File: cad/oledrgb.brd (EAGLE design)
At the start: 27.5 x 29.5 mm, 17 parts, among them U1 FAN5331SX

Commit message: embiggen connector
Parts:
- removed CN1: (no value), jaw:HEADER-2X04
- added CONN2: HEADER-5X2-PTH, jaw:HEADER-5X2-PTH
- moved R3 2.55 mm to (59.0, 18.5), turned to 180 degrees
- moved C5 0.51 mm to (40.3, 12.5)
- moved C1 0.50 mm to (48.0, 10.5)
- moved C2 0.50 mm to (40.4, 9.00)
- moved C3 0.50 mm to (42.2, 12.5)
- moved C4 0.50 mm to (44.0, 12.5)
- moved D1 0.50 mm to (40.0, 6.00)
- moved L1 0.50 mm to (43.5, 6.00)
- moved R1 0.50 mm to (42.2, 9.00)
- moved R2 0.50 mm to (44.0, 9.00)
- moved U1 0.50 mm to (48.0, 7.50)
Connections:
- new net N$19: CONN2.10
- new net N$4: CONN2.9
- net DPYCS: now also CONN2.7; no longer CN1.7
- net DPYDC: now also CONN2.6; no longer CN1.6
- net GND: now also CONN2.8; no longer CN1.8
- net NRST: now also CONN2.2; no longer CN1.2
- net SPIMISO: now also CONN2.3; no longer CN1.3
- net SPIMOSI: now also CONN2.5; no longer CN1.5
- net SPISCK: now also CONN2.4; no longer CN1.4
- net VCC: now also CONN2.1; no longer CN1.1
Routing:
- net N$20: track 13.4 -> 10.1 mm
- net V12: track 52.2 -> 49.4 mm
- net VCC: track 52.5 -> 54.9 mm
- net DPYDC: track 26.8 -> 25.2 mm
- net DPYCS: track 28.1 -> 26.9 mm
- net SPIMOSI: track 30.3 -> 29.3 mm
- net NRST: track 31.5 -> 30.5 mm
- net SPISCK: track 32.7 -> 31.7 mm
- net GND: track 55.9 -> 56.7 mm
- net N$6: track 14.0 -> 13.5 mm
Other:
- outline, holes or cut-outs redrawn

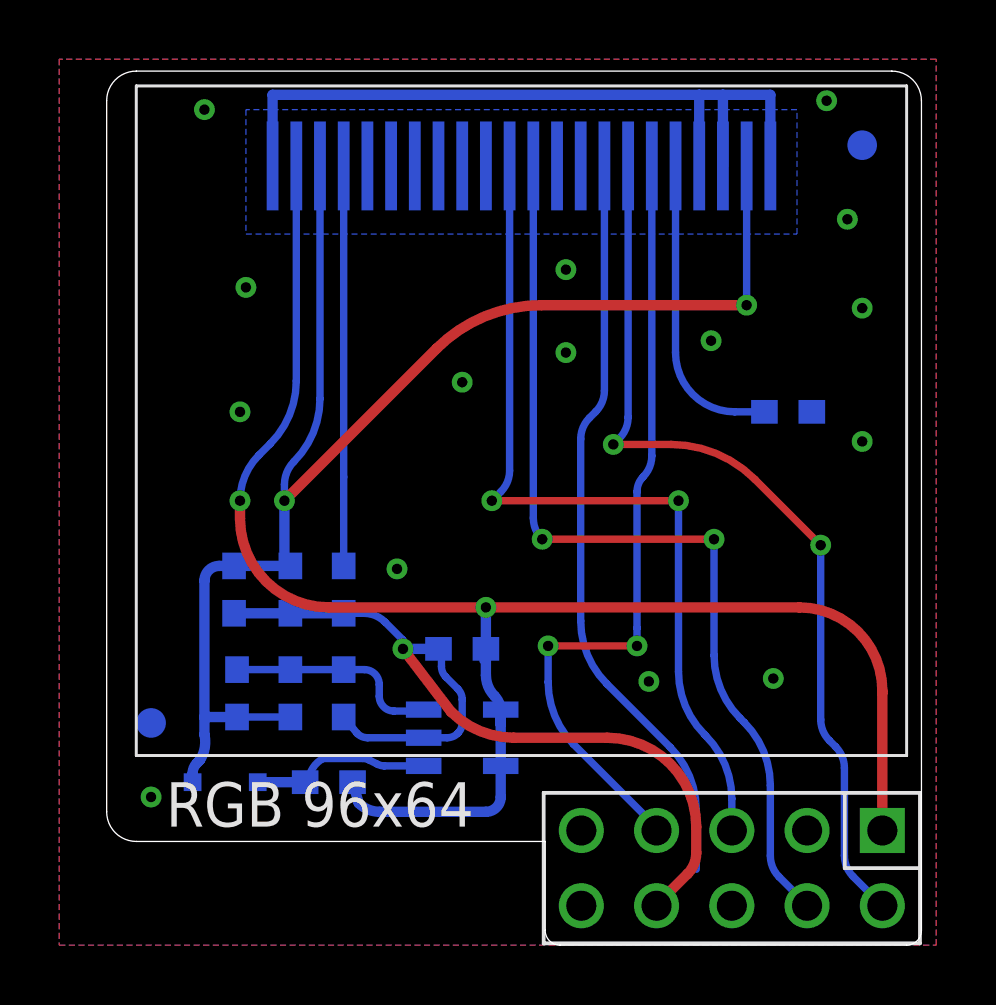
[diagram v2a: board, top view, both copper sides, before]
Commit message: scootch closer to edge
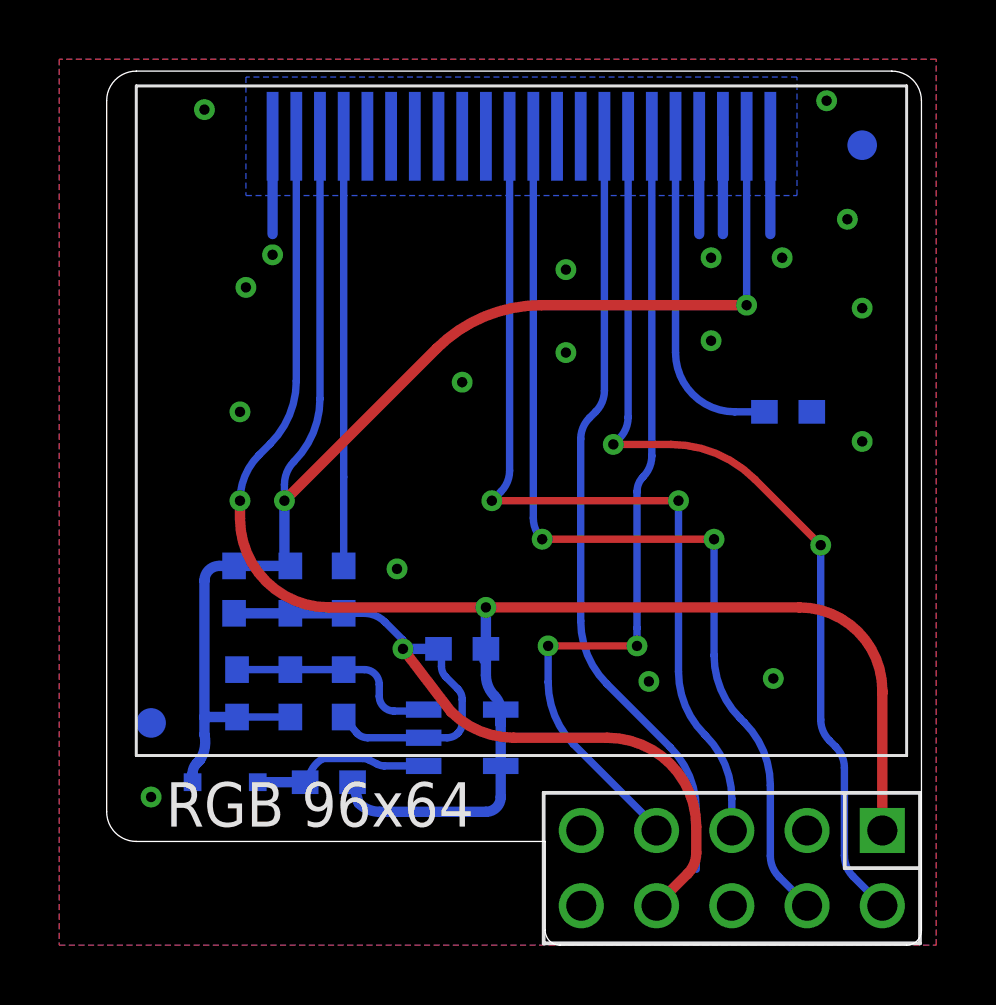
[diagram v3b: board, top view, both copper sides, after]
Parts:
- moved CONN1 1.00 mm to (50.0, 28.0)
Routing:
- net GND: track 56.7 -> 43.5 mm, vias 16 -> 19
- net V12: track 49.4 -> 51.4 mm
- net SPISCK: track 31.7 -> 32.7 mm
- net VCC: track 54.9 -> 55.9 mm
- net SPIMOSI: track 29.3 -> 30.3 mm
- net NRST: track 30.5 -> 31.5 mm
- net N$6: track 13.5 -> 14.5 mm
- net N$20: track 10.1 -> 11.1 mm
- net DPYDC: track 25.2 -> 26.2 mm
- net DPYCS: track 26.9 -> 27.9 mm
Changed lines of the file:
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@@
 <layer number="14" name="Route14" color="1" fill="6" visible="no" active="no"/>
 <layer number="15" name="Route15" color="4" fill="6" visible="no" active="no"/>
-<layer number="16" name="Bottom" color="1" fill="1" visible="no" active="yes"/>
+<layer number="16" name="Bottom" color="1" fill="1" visible="yes" active="yes"/>
 <layer number="17" name="Pads" color="2" fill="1" visible="yes" active="yes"/>
 <layer number="18" name="Vias" color="2" fill="1" visible="yes" active="yes"/>
@@
 <attribute name="VALUE" x="42.586" y="13.978" size="1" layer="28" font="vector" ratio="10" rot="MR270"/>
 </element>
-<element name="CONN1" library="jaw" package="HEADER-22X1-SMD8" value="HEADER-22X1-SMD8" x="50" y="27" rot="MR180"/>
+<element name="CONN1" library="jaw" package="HEADER-22X1-SMD8" value="HEADER-22X1-SMD8" x="50" y="28" rot="MR180"/>
 <element name="D1" library="jaw" package="SOD-323" value="DIODESOD-323" x="40" y="6" smashed="yes" rot="MR180">
 <attribute name="NAME" x="38" y="5.5" size="1" layer="26" ratio="10" rot="MR0"/>
@@
 <wire x1="49.742640625" y1="7.5" x2="47.621321875" y2="8.378678125" width="0.35" layer="1" curve="-44.999958"/>
 <wire x1="47.621321875" y1="8.378678125" x2="46" y2="10.5" width="0.35" layer="1"/>
-<wire x1="41.6" y1="26.8" x2="41.6" y2="29.2" width="0.35" layer="16"/>
-<wire x1="58.4" y1="26.8" x2="58.4" y2="29.2" width="0.35" layer="16"/>
-<wire x1="41.6" y1="29.2" x2="56" y2="29.2" width="0.35" layer="16"/>
-<wire x1="56" y1="26.8" x2="56" y2="29.2" width="0.35" layer="16"/>
-<wire x1="56" y1="29.2" x2="56.8" y2="29.2" width="0.35" layer="16"/>
-<wire x1="56.8" y1="26.8" x2="56.8" y2="29.2" width="0.35" layer="16"/>
-<wire x1="56.8" y1="29.2" x2="58.4" y2="29.2" width="0.35" layer="16"/>
+<wire x1="41.6" y1="27.8" x2="41.6" y2="24.5" width="0.35" layer="16"/>
+<wire x1="58.4" y1="27.8" x2="58.4" y2="24.5" width="0.35" layer="16"/>
+<wire x1="56" y1="27.8" x2="56" y2="24.5" width="0.35" layer="16"/>
+<wire x1="56.8" y1="27.8" x2="56.8" y2="24.5" width="0.35" layer="16"/>
 <polygon width="0.25" layer="16" spacing="0.8" pour="hatch" isolate="0.25">
 <vertex x="34.4" y="30.4"/>
@@
 <wire x1="47.3" y1="9.90710625" x2="47.3" y2="10.4" width="0.25" layer="16"/>
 <wire x1="47.3" y1="10.4" x2="47.2" y2="10.5" width="0.25" layer="16"/>
-<wire x1="58.4" y1="29.2" x2="60.3" y2="29" width="0" layer="19" extent="16-16"/>
-<wire x1="39.3" y1="28.7" x2="41.6" y2="29.2" width="0" layer="19" extent="16-16"/>
-<wire x1="61" y1="25" x2="58.4" y2="26.8" width="0" layer="19" extent="16-16"/>
-<wire x1="61.5" y1="22" x2="61" y2="25" width="0" layer="19" extent="1-1"/>
-<wire x1="59.8" y1="18.5" x2="61.5" y2="22" width="0" layer="19" extent="16-16"/>
-<wire x1="61.5" y1="17.5" x2="59.8" y2="18.5" width="0" layer="19" extent="16-16"/>
-<wire x1="56.4" y1="20.9" x2="59.8" y2="18.5" width="0" layer="19" extent="16-16"/>
-<wire x1="40.7" y1="22.7" x2="41.6" y2="26.8" width="0" layer="19" extent="16-16"/>
-<wire x1="40.5" y1="18.5" x2="40.7" y2="22.7" width="0" layer="19" extent="1-1"/>
-<wire x1="51.5" y1="20.5" x2="56.4" y2="20.9" width="0" layer="19" extent="1-1"/>
-<wire x1="51.5" y1="23.3" x2="51.5" y2="20.5" width="0" layer="19" extent="1-1"/>
-<wire x1="48" y1="19.5" x2="51.5" y2="20.5" width="0" layer="19" extent="1-1"/>
-<wire x1="45.8" y1="13.2" x2="48" y2="19.5" width="0" layer="19" extent="1-1"/>
-<wire x1="45.39289375" y1="11.40710625" x2="45.8" y2="13.2" width="0" layer="19" extent="16-16"/>
-<wire x1="54.56" y1="1.83" x2="54.6" y2="1.9" width="0" layer="19" extent="1-1"/>
-<wire x1="54.3" y1="9.4" x2="52.9" y2="7.5" width="0" layer="19" extent="1-1"/>
-<wire x1="58.5" y1="9.5" x2="54.3" y2="9.4" width="0" layer="19" extent="1-1"/>
-<wire x1="37.5" y1="5.5" x2="40.3" y2="11.7" width="0" layer="19" extent="16-16"/>
+<via x="41.6" y="23.8" extent="1-16" drill="0.35"/>
+<via x="56.4" y="23.7" extent="1-16" drill="0.35"/>
+<via x="58.8" y="23.7" extent="1-16" drill="0.35"/>
 </signal>
 <signal name="VCC">
@@
 <wire x1="59.38" y1="11.9" x2="62.18" y2="9.1" width="0.35" layer="1" curve="-90"/>
 <via x="48.8" y="11.9" extent="1-16" drill="0.35"/>
-<wire x1="42.4" y1="26.8" x2="42.4" y2="19.542640625" width="0.25" layer="16"/>
+<wire x1="42.4" y1="27.8" x2="42.4" y2="19.542640625" width="0.25" layer="16"/>
 <wire x1="42.4" y1="19.542640625" x2="41.521321875" y2="17.421321875" width="0.25" layer="16" curve="-44.999958"/>
 <wire x1="41.521321875" y1="17.421321875" x2="41.136396875" y2="17.036396875" width="0.25" layer="16"/>
@@
 <wire x1="62.18" y1="9.1" x2="62.18" y2="9" width="0.35" layer="1"/>
 <wire x1="62.18" y1="9" x2="62.18" y2="4.37" width="0.35" layer="1"/>
-<wire x1="62.18" y1="12.12" x2="62.18" y2="9.1" width="0" layer="19" extent="1-16"/>
-<wire x1="62.18" y1="9.1" x2="62.18" y2="9.1" width="0" layer="19" extent="1-16"/>
-<wire x1="62.18" y1="9.1" x2="62.18" y2="9" width="0" layer="19" extent="1-16"/>
-<wire x1="62.18" y1="12.12" x2="62.18" y2="12.491571875" width="0" layer="19" extent="1-16"/>
-<wire x1="62.18" y1="12.491571875" x2="61.5942125" y2="13.9057875" width="0" layer="19" curve="45.000063" extent="1-16"/>
-<wire x1="61.5942125" y1="13.9057875" x2="61.5857875" y2="13.9142125" width="0" layer="19" extent="1-16"/>
-<wire x1="61.5857875" y1="13.9142125" x2="60.171571875" y2="14.5" width="0" layer="19" curve="45.00009" extent="1-16"/>
 </signal>
 <signal name="NRST">
@@
 <wire x1="61.19289375" y1="2.81710625" x2="62.18" y2="1.83" width="0.25" layer="16"/>
 <contactref element="CONN1" pad="16"/>
-<wire x1="53.6" y1="26.8" x2="53.6" y2="18.3142125" width="0.25" layer="16"/>
+<wire x1="53.6" y1="27.8" x2="53.6" y2="18.3142125" width="0.25" layer="16"/>
 <wire x1="53.6" y1="18.3142125" x2="53.30710625" y2="17.60710625" width="0.25" layer="16" curve="-45"/>
 <wire x1="53.30710625" y1="17.60710625" x2="53.1" y2="17.4" width="0.25" layer="16"/>
@@
 <signal name="DPYDC">
 <contactref element="CONN1" pad="15"/>
-<wire x1="52.8" y1="26.8" x2="52.8" y2="19.2142125" width="0.25" layer="16"/>
+<wire x1="52.8" y1="27.8" x2="52.8" y2="19.2142125" width="0.25" layer="16"/>
 <wire x1="52.8" y1="19.2142125" x2="52.50710625" y2="18.50710625" width="0.25" layer="16" curve="-45"/>
 <wire x1="52.50710625" y1="18.50710625" x2="52.29289375" y2="18.29289375" width="0.25" layer="16"/>
@@
 <signal name="SPISCK">
 <contactref element="CONN1" pad="12"/>
-<wire x1="50.4" y1="26.8" x2="50.4" y2="14.9142125" width="0.25" layer="16"/>
+<wire x1="50.4" y1="27.8" x2="50.4" y2="14.9142125" width="0.25" layer="16"/>
 <wire x1="50.4" y1="14.9142125" x2="50.69289375" y2="14.20710625" width="0.25" layer="16" curve="45"/>
 <wire x1="50.69289375" y1="14.20710625" x2="50.7" y2="14.2" width="0.25" layer="16"/>
@@
 <signal name="SPIMOSI">
 <contactref element="CONN1" pad="11"/>
-<wire x1="49.6" y1="26.8" x2="49.6" y2="16.5142125" width="0.25" layer="16"/>
+<wire x1="49.6" y1="27.8" x2="49.6" y2="16.5142125" width="0.25" layer="16"/>
 <wire x1="49.6" y1="16.5142125" x2="49.30710625" y2="15.80710625" width="0.25" layer="16" curve="-45"/>
 <wire x1="49.30710625" y1="15.80710625" x2="49" y2="15.5" width="0.25" layer="16"/>
@@
 <signal name="DPYCS">
 <contactref element="CONN1" pad="17"/>
-<wire x1="54.4" y1="26.8" x2="54.4" y2="17.0142125" width="0.25" layer="16"/>
+<wire x1="54.4" y1="27.8" x2="54.4" y2="17.0142125" width="0.25" layer="16"/>
 <wire x1="54.4" y1="17.0142125" x2="54.10710625" y2="16.30710625" width="0.25" layer="16" curve="-45"/>
 <wire x1="54.10710625" y1="16.30710625" x2="53.9" y2="15.80710625" width="0.25" layer="16" curve="45"/>
@@
 <contactref element="C5" pad="1"/>
 <wire x1="42.2" y1="8.2" x2="40.4" y2="8.2" width="0.25" layer="16"/>
-<wire x1="43.2" y1="26.8" x2="43.2" y2="18.942640625" width="0.25" layer="16"/>
+<wire x1="43.2" y1="27.8" x2="43.2" y2="18.942640625" width="0.25" layer="16"/>
 <wire x1="43.2" y1="18.942640625" x2="42.321321875" y2="16.821321875" width="0.25" layer="16" curve="-44.999958"/>
 <wire x1="42.321321875" y1="16.821321875" x2="42" y2="16.04558125" width="0.25" layer="16" curve="45"/>
 <wire x1="42" y1="16.04558125" x2="42" y2="15.5" width="0.25" layer="16"/>
-<wire x1="57.6" y1="26.8" x2="57.6" y2="22.1" width="0.25" layer="16"/>
+<wire x1="57.6" y1="27.8" x2="57.6" y2="22.1" width="0.25" layer="16"/>
 <via x="57.6" y="22.1" extent="1-16" drill="0.35"/>
 <wire x1="57.6" y1="22.1" x2="50.67106875" y2="22.1" width="0.35" layer="1"/>
@@
 <contactref element="CONN1" pad="4"/>
 <contactref element="C4" pad="2"/>
-<wire x1="44" y1="26.8" x2="44" y2="17.6" width="0.25" layer="16"/>
+<wire x1="44" y1="27.8" x2="44" y2="17.6" width="0.25" layer="16"/>
 <wire x1="44" y1="17.6" x2="44" y2="16.3" width="0.25" layer="16"/>
 <wire x1="44" y1="16.3" x2="44" y2="13.3" width="0.25" layer="16"/>
@@
 <contactref element="CONN1" pad="18"/>
 <contactref element="R3" pad="1"/>
-<wire x1="55.2" y1="26.8" x2="55.2" y2="20.5" width="0.25" layer="16"/>
+<wire x1="55.2" y1="27.8" x2="55.2" y2="20.5" width="0.25" layer="16"/>
 <wire x1="55.2" y1="20.5" x2="57.2" y2="18.5" width="0.25" layer="16" curve="90"/>
 <wire x1="57.2" y1="18.5" x2="58.2" y2="18.5" width="0.25" layer="16"/>
@@
 <signal name="N$2">
 <polygon width="0.25" layer="16" pour="cutout">
-<vertex x="40.7" y="28.7"/>
-<vertex x="40.7" y="24.5"/>
-<vertex x="59.3" y="24.5"/>
-<vertex x="59.3" y="28.7"/>
+<vertex x="40.7" y="29.8"/>
+<vertex x="40.7" y="25.8"/>
+<vertex x="59.3" y="25.8"/>
+<vertex x="59.3" y="29.8"/>
 </polygon>
 </signal>
